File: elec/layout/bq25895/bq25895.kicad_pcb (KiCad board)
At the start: 2 copper layers, 24 parts, among them U1 ?, U2 ?, U3 ?

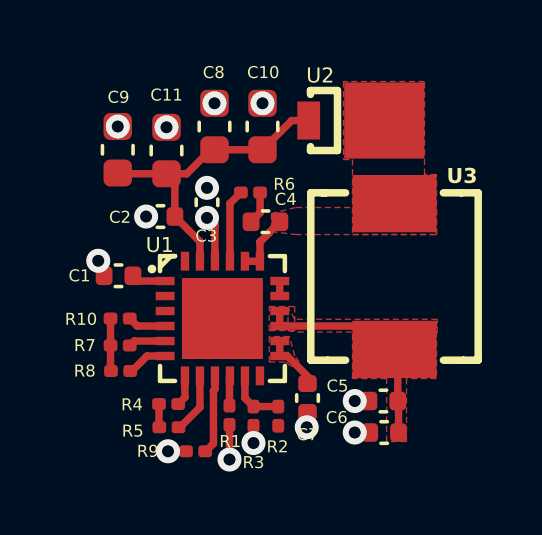
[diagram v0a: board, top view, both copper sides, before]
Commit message: rebuilt, some layout changes
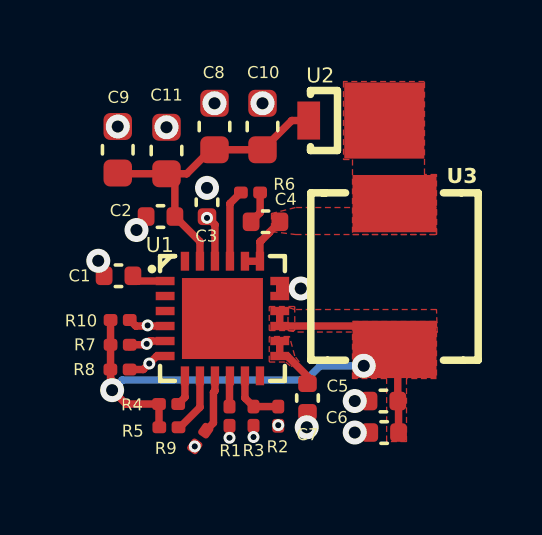
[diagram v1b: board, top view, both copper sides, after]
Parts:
- C4: value 50V 47nF X7R ±10% 0402 Multilayer Ceramic Capacitors MLCC - SMD/SMT ROHS -> 50V 47nF X7R ±10% 0402 Multilayer Ceramic Capacitors MLCC - SMD/SMT ROHS
- R1: value 50mW Thick Film Resistors 25V ±1% ±200ppm/℃ 120Ω 0201 Chip Resistor - Surface Mount ROHS -> 50mW Thick Film Resistors ±1% ±200ppm/℃ 127Ω 0201 Chip Resistor - Surface Mount ROHS
- R6: value 50mW Thick Film Resistors 25V ±5% 0Ω 0201 Chip Resistor - Surface Mount ROHS -> 50mW Thick Film Resistors 25V ±1% 0Ω 0201 Chip Resistor - Surface Mount ROHS
- moved R9 0.45 mm to (150.1, 92.8), turned to -125 degrees
- moved R8 0.05 mm to (147.4, 90.5)
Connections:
- U1 pad 25: pad -> gnd
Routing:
- net vcc-3: track 9.83 -> 21.4 mm, vias 0 -> 2
- net regn: track 1.63 -> 9.53 mm, vias 1 -> 2
- net ce: track 2.66 -> 1.95 mm
- net scl: track 1.24 -> 1.48 mm, vias 0 -> 1
- net gnd: track 4.89 -> 4.94 mm, vias 13 -> 14
- net (no net): vias 0 -> 2
- added copper zone on F.Cu, net (none)
- removed copper zone on F.Cu, net sw
- removed copper zone on F.Cu, net vcc-2
- removed copper zone on F.Cu, net vcc-3
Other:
- copper layers 2 -> 4
